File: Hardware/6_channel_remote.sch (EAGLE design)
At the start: 13 parts, among them J1 46765-0001

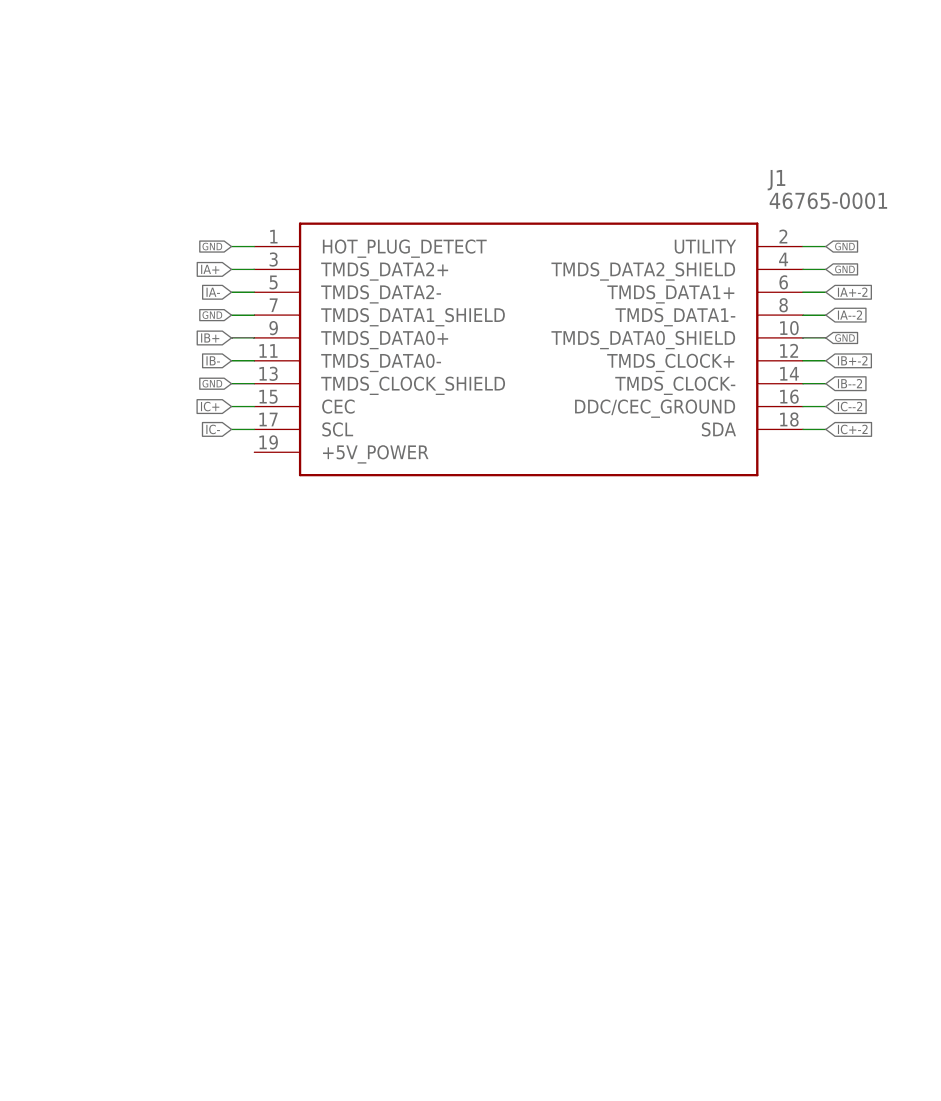
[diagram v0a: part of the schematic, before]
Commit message: v1.1 remote
- changed micro-hdmi connector to through-hole
- added mini-hdmi connector option
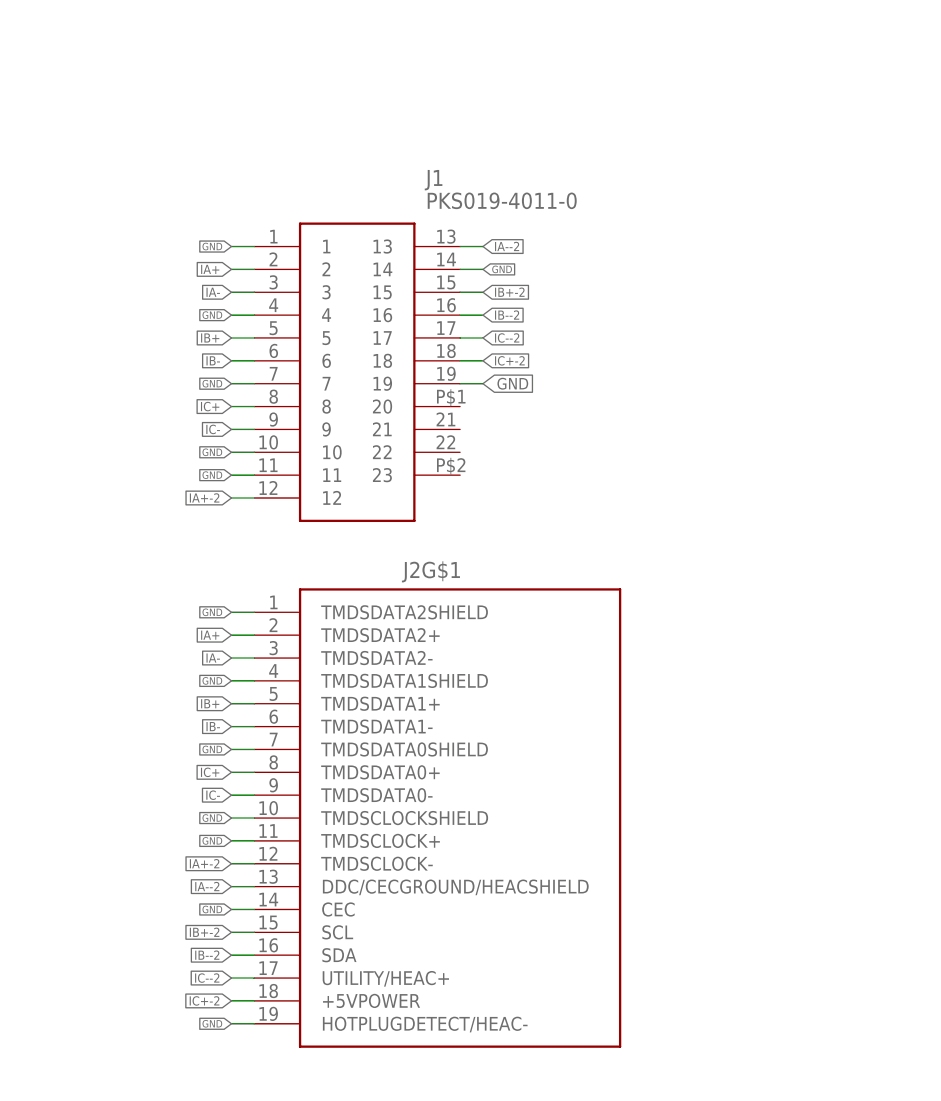
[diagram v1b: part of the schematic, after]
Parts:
- added J2: (no value), Wurth_Elektronik_Electromechanic_Input-Output_Connectors_rev19a:685119136923
- J1: value 46765-0001 -> PKS019-4011-0; device 46765-0001:46765-0001 -> SamacSys_Parts:PKS019-4011-0
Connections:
- net GND: now also J1.1, J1.10, J1.11, J1.14, J1.19, J1.4, J1.7, J2G$1.CEC, J2G$1.HOTPLUGDETECT/HEAC-, J2G$1.TMDSCLOCK+, J2G$1.TMDSCLOCKSHIELD, J2G$1.TMDSDATA0SHIELD, J2G$1.TMDSDATA1SHIELD, J2G$1.TMDSDATA2SHIELD; no longer J1.HOT_PLUG_DETECT, J1.TMDS_CLOCK_SHIELD, J1.TMDS_DATA0_SHIELD, J1.TMDS_DATA1_SHIELD, J1.TMDS_DATA2_SHIELD, J1.UTILITY
- net IA+: now also J1.2, J2G$1.TMDSDATA2+; no longer J1.TMDS_DATA2+
- net IA+-2: now also J1.12, J2G$1.TMDSCLOCK-; no longer J1.TMDS_DATA1+
- net IA-: now also J1.3, J2G$1.TMDSDATA2-; no longer J1.TMDS_DATA2-
- net IA--2: now also J1.13, J2G$1.DDC/CECGROUND/HEACSHIELD; no longer J1.TMDS_DATA1-
- net IB+: now also J1.5, J2G$1.TMDSDATA1+; no longer J1.TMDS_DATA0+
- net IB+-2: now also J1.15, J2G$1.SCL; no longer J1.TMDS_CLOCK+
- net IB-: now also J1.6, J2G$1.TMDSDATA1-; no longer J1.TMDS_DATA0-
- net IB--2: now also J1.16, J2G$1.SDA; no longer J1.TMDS_CLOCK-
- net IC+: now also J1.8, J2G$1.TMDSDATA0+; no longer J1.CEC
- net IC+-2: now also J1.18, J2G$1.+5VPOWER; no longer J1.SDA
- net IC-: now also J1.9, J2G$1.TMDSDATA0-; no longer J1.SCL
- net IC--2: now also J1.17, J2G$1.UTILITY/HEAC+; no longer J1.DDC/CEC_GROUND
